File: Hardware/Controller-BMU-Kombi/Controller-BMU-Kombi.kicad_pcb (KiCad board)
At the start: 2 copper layers, 15 parts, among them J1 Conn_01x05_Socket, J2 Conn_01x05_Socket, J3 Conn_01x05_Socket, J4 Conn_01x05_Socket, J5 Conn_01x05_Socket, J6 Conn_01x05_Socket, U2 ESP32_NODEMCU

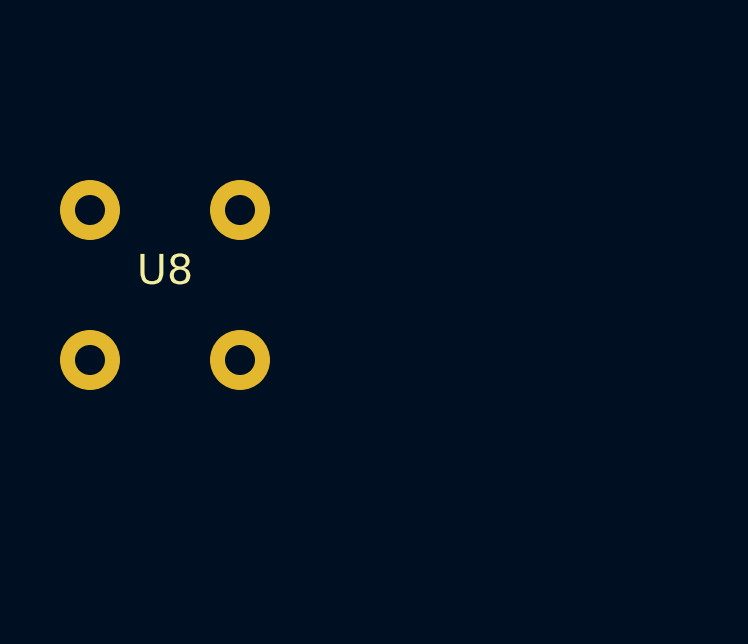
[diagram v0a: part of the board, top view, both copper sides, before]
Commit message: added servo connectors
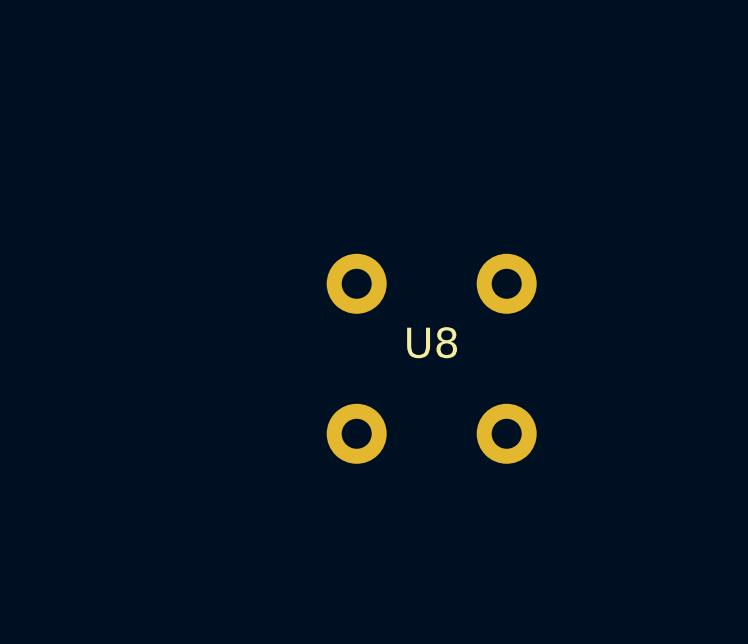
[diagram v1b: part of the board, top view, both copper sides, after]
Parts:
- moved U8 9.22 mm to (62.3, 104.1)
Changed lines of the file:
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@@
 	(footprint "Batteriestecker:Batteriestecker"
 		(layer "F.Cu")
-		(at 53.38 101.64)
+		(at 62.27 104.1)
 		(property "Reference" "U8"
 			(at 0 -0.5 0)
@@
 		)
 		(fp_text user "${REFERENCE}"
-			(at -5.775 5.08 360)
+			(at -5.775 5.08 0)
 			(layer "F.Fab")
 			(effects
@@
 		)
 		(fp_text user "${REFERENCE}"
-			(at -5.775 5.08 360)
+			(at -5.775 5.08 0)
 			(layer "F.Fab")
 			(effects
@@
 		(at 148.29 109.22 180)
 		(property "Reference" "U2"
-			(at -11.075 -29.385 360)
+			(at -11.075 -29.385 0)
 			(layer "F.SilkS")
 			(effects
@@
 		)
 		(property "Value" "ESP32_NODEMCU"
-			(at -1.55 29.385 360)
+			(at -1.55 29.385 0)
 			(layer "F.Fab")
 			(effects
@@
 		)
 		(property "Footprint" "ESP32_NODEMCU:MODULE_ESP32_NODEMCU"
-			(at 0 0 360)
+			(at 0 0 0)
 			(layer "F.Fab")
 			(hide yes)
@@
 		)
 		(property "Datasheet" ""
-			(at 0 0 360)
+			(at 0 0 0)
 			(layer "F.Fab")
 			(hide yes)
@@
 		)
 		(property "Description" ""
-			(at 0 0 360)
+			(at 0 0 0)
 			(layer "F.Fab")
 			(hide yes)

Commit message: added gerber files
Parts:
- added J10: Conn_01x03_Pin, Connector_PinHeader_2.54mm:PinHeader_1x03_P2.54mm_Vertical, F.Cu at (64.7, 64.5)
- added J11: Conn_01x03_Pin, Connector_PinHeader_2.54mm:PinHeader_1x03_P2.54mm_Vertical, F.Cu at (69.3, 64.5)
- added J12: Conn_01x03_Pin, Connector_PinHeader_2.54mm:PinHeader_1x03_P2.54mm_Vertical, F.Cu at (74.0, 64.5)
- added J13: Conn_01x03_Pin, Connector_PinHeader_2.54mm:PinHeader_1x03_P2.54mm_Vertical, F.Cu at (50.8, 74.2)
- added J14: Conn_01x03_Pin, Connector_PinHeader_2.54mm:PinHeader_1x03_P2.54mm_Vertical, F.Cu at (55.4, 74.2)
- added J15: Conn_01x03_Pin, Connector_PinHeader_2.54mm:PinHeader_1x03_P2.54mm_Vertical, F.Cu at (60.0, 74.2)
- added J16: Conn_01x03_Pin, Connector_PinHeader_2.54mm:PinHeader_1x03_P2.54mm_Vertical, F.Cu at (64.7, 74.2)
- added J17: Conn_01x03_Pin, Connector_PinHeader_2.54mm:PinHeader_1x03_P2.54mm_Vertical, F.Cu at (69.3, 74.2)
- added J18: Conn_01x03_Pin, Connector_PinHeader_2.54mm:PinHeader_1x03_P2.54mm_Vertical, F.Cu at (74.0, 74.2)
- added J19: Conn_01x03_Pin, Connector_PinHeader_2.54mm:PinHeader_1x03_P2.54mm_Vertical, F.Cu at (50.8, 83.9)
- added J20: Conn_01x03_Pin, Connector_PinHeader_2.54mm:PinHeader_1x03_P2.54mm_Vertical, F.Cu at (55.4, 83.9)
- added J21: Conn_01x03_Pin, Connector_PinHeader_2.54mm:PinHeader_1x03_P2.54mm_Vertical, F.Cu at (60.0, 83.9)
- added J22: Conn_01x03_Pin, Connector_PinHeader_2.54mm:PinHeader_1x03_P2.54mm_Vertical, F.Cu at (64.7, 83.9)
- added J23: Conn_01x03_Pin, Connector_PinHeader_2.54mm:PinHeader_1x03_P2.54mm_Vertical, F.Cu at (69.3, 83.9)
- added J24: Conn_01x03_Pin, Connector_PinHeader_2.54mm:PinHeader_1x03_P2.54mm_Vertical, F.Cu at (74.0, 83.9)
- added J7: Conn_01x03_Pin, Connector_PinHeader_2.54mm:PinHeader_1x03_P2.54mm_Vertical, F.Cu at (50.8, 64.5)
- added J8: Conn_01x03_Pin, Connector_PinHeader_2.54mm:PinHeader_1x03_P2.54mm_Vertical, F.Cu at (55.4, 64.5)
- added J9: Conn_01x03_Pin, Connector_PinHeader_2.54mm:PinHeader_1x03_P2.54mm_Vertical, F.Cu at (60.0, 64.5)
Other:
- board outline added: 184.5 x 81.5 mm

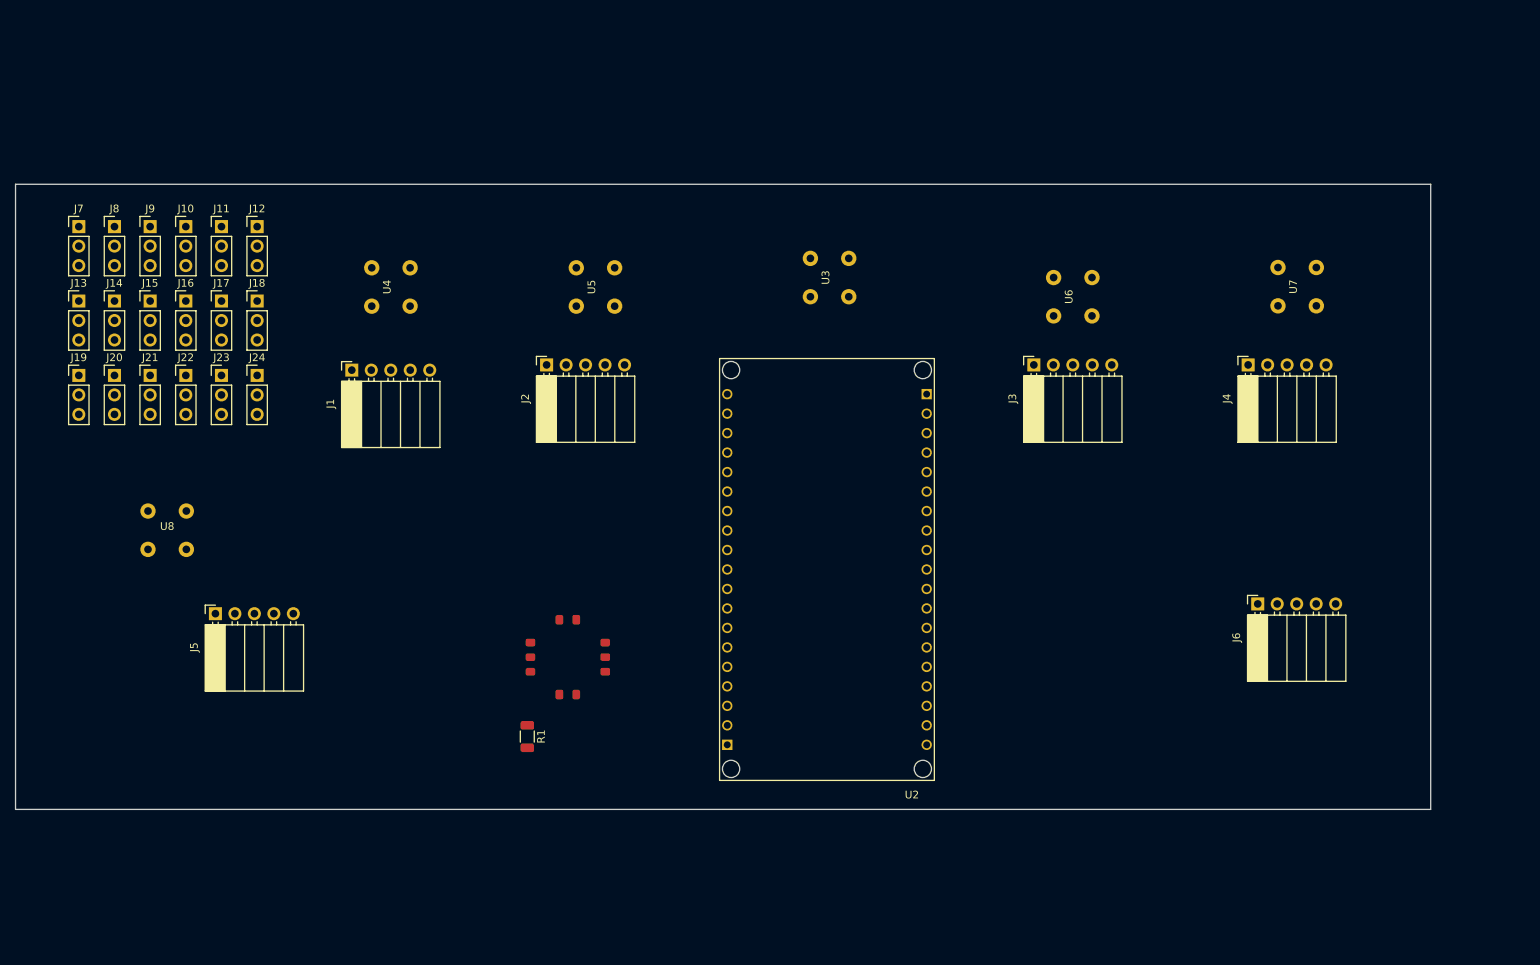
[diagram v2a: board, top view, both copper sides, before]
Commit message: added rf connectors, changed a few net labels
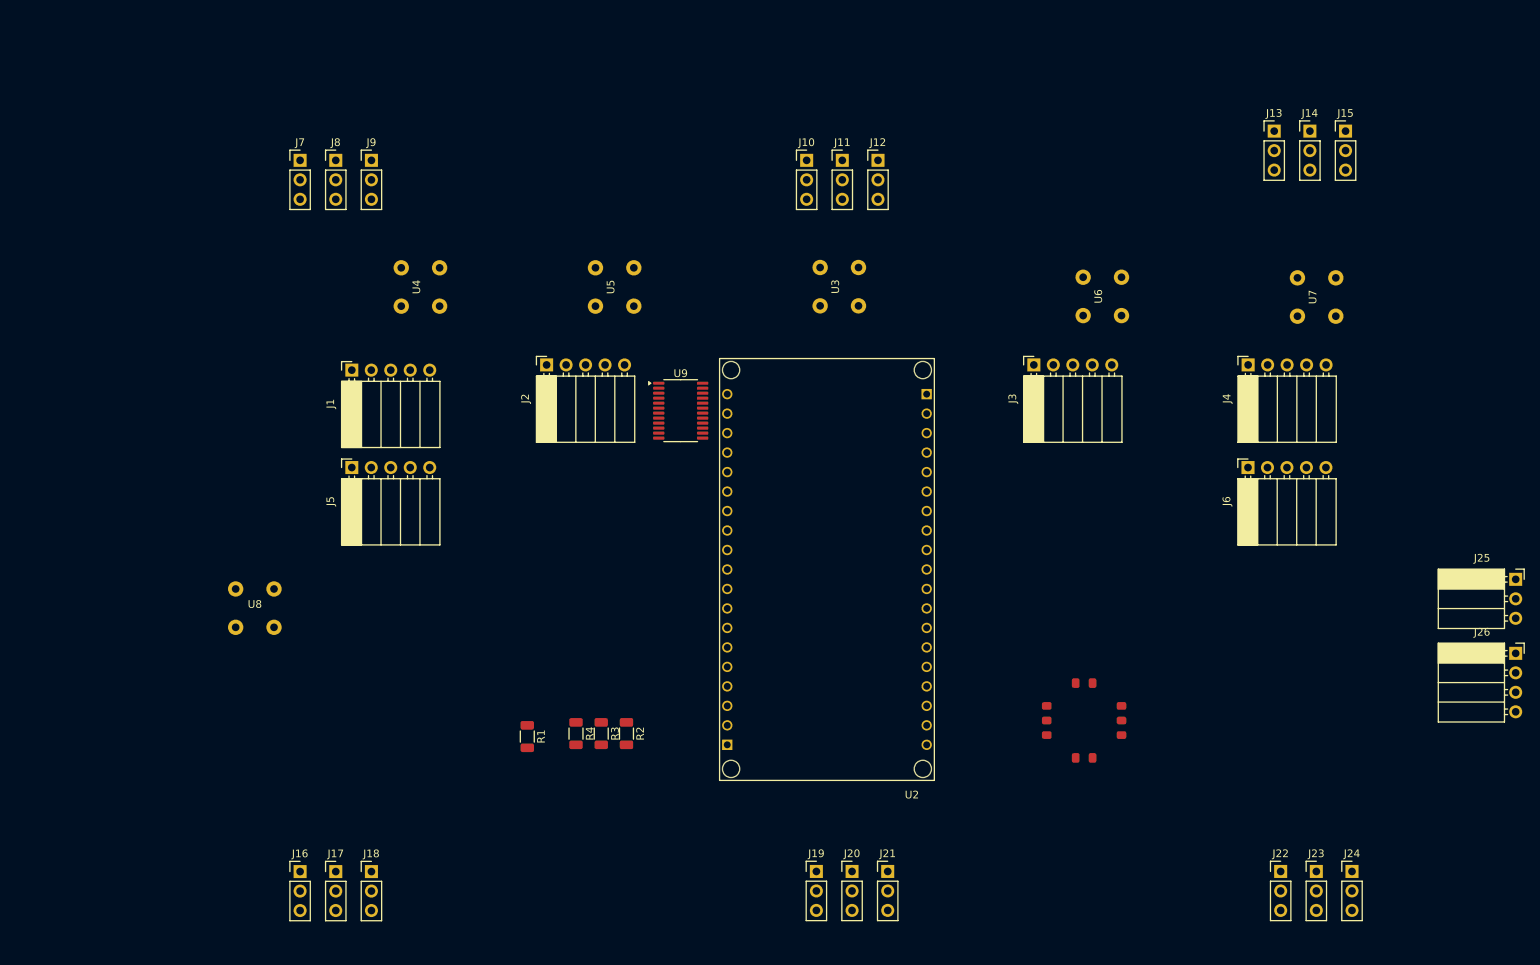
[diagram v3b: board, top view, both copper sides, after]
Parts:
- added J25: Conn_01x03_Socket, Connector_PinSocket_2.54mm:PinSocket_1x03_P2.54mm_Horizontal, F.Cu at (238.1, 110.5)
- added J26: Conn_01x04_Socket, Connector_PinSocket_2.54mm:PinSocket_1x04_P2.54mm_Horizontal, F.Cu at (238.1, 120.2)
- added R2: 10k, Resistor_SMD:R_1206_3216Metric, F.Cu at (122.2, 130.6)
- added R3: 10k, Resistor_SMD:R_1206_3216Metric, F.Cu at (118.9, 130.6)
- added R4: 10k, Resistor_SMD:R_1206_3216Metric, F.Cu at (115.6, 130.6)
- added U9: PCA9555PW, Package_SO:TSSOP-24_4.4x7.8mm_P0.65mm, F.Cu at (129.2, 88.5)
- moved J15 157.4 mm to (215.9, 52.1)
- moved J13 157.4 mm to (206.6, 52.1)
- moved J14 157.4 mm to (211.2, 52.1)
- moved J22 156.7 mm to (207.4, 148.6)
- moved J23 156.7 mm to (212.1, 148.6)
- moved J24 156.7 mm to (216.7, 148.6)
- moved J19 115.9 mm to (146.9, 148.6)
- moved J20 115.9 mm to (151.6, 148.6)
- moved J21 115.9 mm to (156.2, 148.6)
- moved J11 81.4 mm to (150.3, 55.9)
- moved J12 81.4 mm to (154.9, 55.9)
- moved J10 81.4 mm to (145.6, 55.9)
- moved J17 75.9 mm to (84.2, 148.6)
- moved J18 75.9 mm to (88.9, 148.6)
- moved J16 75.9 mm to (79.6, 148.6)
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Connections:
- J10 pad 1: unconnected-(J10-Pin_1-Pad1) -> +5V
- J10 pad 2: unconnected-(J10-Pin_2-Pad2) -> SERV4
- J10 pad 3: unconnected-(J10-Pin_3-Pad3) -> GND
- J11 pad 1: unconnected-(J11-Pin_1-Pad1) -> +5V
- J11 pad 2: unconnected-(J11-Pin_2-Pad2) -> SERV5
- J11 pad 3: unconnected-(J11-Pin_3-Pad3) -> GND
- J12 pad 1: unconnected-(J12-Pin_1-Pad1) -> +5V
- J12 pad 2: unconnected-(J12-Pin_2-Pad2) -> SERV6
- J12 pad 3: unconnected-(J12-Pin_3-Pad3) -> GND
- J13 pad 1: unconnected-(J13-Pin_1-Pad1) -> +5V
- J13 pad 2: unconnected-(J13-Pin_2-Pad2) -> SERV7
- J13 pad 3: unconnected-(J13-Pin_3-Pad3) -> GND
- J14 pad 1: unconnected-(J14-Pin_1-Pad1) -> +5V
- J14 pad 2: unconnected-(J14-Pin_2-Pad2) -> SERV8
- J14 pad 3: unconnected-(J14-Pin_3-Pad3) -> GND
- J15 pad 1: unconnected-(J15-Pin_1-Pad1) -> +5V
- J15 pad 2: unconnected-(J15-Pin_2-Pad2) -> SERV10
- J15 pad 3: unconnected-(J15-Pin_3-Pad3) -> GND
- J16 pad 1: unconnected-(J16-Pin_1-Pad1) -> +5V
- J16 pad 2: unconnected-(J16-Pin_2-Pad2) -> SERV11
- J16 pad 3: unconnected-(J16-Pin_3-Pad3) -> GND
- J17 pad 1: unconnected-(J17-Pin_1-Pad1) -> +5V
- J17 pad 2: unconnected-(J17-Pin_2-Pad2) -> SERV12
- J17 pad 3: unconnected-(J17-Pin_3-Pad3) -> GND
- J18 pad 1: unconnected-(J18-Pin_1-Pad1) -> +5V
- J18 pad 2: unconnected-(J18-Pin_2-Pad2) -> SERV13
- J18 pad 3: unconnected-(J18-Pin_3-Pad3) -> GND
- J19 pad 1: unconnected-(J19-Pin_1-Pad1) -> +5V
- J19 pad 2: unconnected-(J19-Pin_2-Pad2) -> SERV14
- J19 pad 3: unconnected-(J19-Pin_3-Pad3) -> GND
- J20 pad 1: unconnected-(J20-Pin_1-Pad1) -> +5V
- J20 pad 2: unconnected-(J20-Pin_2-Pad2) -> SERV15
- J20 pad 3: unconnected-(J20-Pin_3-Pad3) -> GND
- J21 pad 1: unconnected-(J21-Pin_1-Pad1) -> +5V
- J21 pad 2: unconnected-(J21-Pin_2-Pad2) -> SERV16
- J21 pad 3: unconnected-(J21-Pin_3-Pad3) -> GND
- J22 pad 1: unconnected-(J22-Pin_1-Pad1) -> +5V
- J22 pad 2: unconnected-(J22-Pin_2-Pad2) -> SERV17
- J22 pad 3: unconnected-(J22-Pin_3-Pad3) -> GND
- J23 pad 1: unconnected-(J23-Pin_1-Pad1) -> +5V
- J23 pad 2: unconnected-(J23-Pin_2-Pad2) -> SERV9
- J23 pad 3: unconnected-(J23-Pin_3-Pad3) -> GND
- J24 pad 1: unconnected-(J24-Pin_1-Pad1) -> +5V
- J24 pad 2: unconnected-(J24-Pin_2-Pad2) -> SERV18
- J24 pad 3: unconnected-(J24-Pin_3-Pad3) -> GND
- J7 pad 1: unconnected-(J7-Pin_1-Pad1) -> +5V
- J7 pad 2: unconnected-(J7-Pin_2-Pad2) -> SERV1
- J7 pad 3: unconnected-(J7-Pin_3-Pad3) -> GND
- J8 pad 1: unconnected-(J8-Pin_1-Pad1) -> +5V
- J8 pad 2: unconnected-(J8-Pin_2-Pad2) -> SERV2
- J8 pad 3: unconnected-(J8-Pin_3-Pad3) -> GND
- J9 pad 1: unconnected-(J9-Pin_1-Pad1) -> +5V
- J9 pad 2: unconnected-(J9-Pin_2-Pad2) -> SERV3
- J9 pad 3: unconnected-(J9-Pin_3-Pad3) -> GND
- U2 pad J4_11: unconnected-(U2-G17-PadJ4_11) -> BUT5
- U2 pad J4_12: unconnected-(U2-G16-PadJ4_12) -> DATA
- U2 pad J4_13: unconnected-(U2-G4-PadJ4_13) -> SERV17
- U2 pad J4_3: BUT3 -> SCL
- U2 pad J4_6: BUT4 -> SDA
- U2 pad J4_8: BUT5 -> BUT3
- U2 pad J4_9: unconnected-(U2-G18-PadJ4_9) -> BUT4
- U2 pad J5_5: unconnected-(U2-G13-PadJ5_5) -> SERV18
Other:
- board outline removed

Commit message: general pcb layout
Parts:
- added U10: ~, BMU:BMU, F.Cu at (117.5, 115.6)
- added U11: ~, BMU:BMU, F.Cu at (188.6, 115.6)
- added U12: ~, BMU:BMU, F.Cu at (168.2, 115.6)
- added U13: ~, BMU:BMU, F.Cu at (96.9, 115.6)
- added U14: ~, Lokale Bibliothek:Empfänger, F.Cu at (177.8, 88.2)
- added U15: ~, Lokale Bibliothek:Sender, F.Cu at (116.8, 90.2)
- J25, J26, U9: moved to B.Cu
- moved J25 125.5 mm to (119.4, 69.8), turned to 90 degrees
- moved J9 103.1 mm to (128.3, 151.1)
- moved J8 95.8 mm to (128.3, 141.0)
- moved U1 92.8 mm to (96.9, 91.5)
- moved J7 89.3 mm to (128.3, 130.8)
- moved J26 83.5 mm to (171.5, 69.8), turned to 90 degrees
- moved J10 80.3 mm to (139.3, 135.9)
- moved J11 80.3 mm to (143.9, 135.9)
- moved J12 80.3 mm to (148.6, 135.9)
- moved J15 43.0 mm to (201.9, 92.7)
- moved J6 35.9 mm to (184.1, 126.4)
- moved R2 32.6 mm to (103.3, 104.0)
- moved R3 32.6 mm to (100.0, 104.0)
- moved R4 32.6 mm to (96.7, 104.0)
- moved R1 32.6 mm to (90.3, 104.4)
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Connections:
- J26 pad 1: +5V -> GND
- J26 pad 2: unconnected-(J26-Pin_2-Pad2) -> DATA
- J26 pad 4: GND -> +5V
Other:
- board outline added: 129.5 x 109.2 mm
